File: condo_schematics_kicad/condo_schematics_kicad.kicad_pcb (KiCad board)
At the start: 2 copper layers, 40.6 x 30.5 mm, 3 parts, among them J1 Conn_01x02_Male

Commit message: Adding kicad schematics and PCB
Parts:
- added J10: Conn_01x01_Male, Connector_PinHeader_2.54mm:PinHeader_1x01_P2.54mm_Vertical, F.Cu at (132.1, 109.2)
- added J11: Conn_01x01_Male, Connector_PinHeader_2.54mm:PinHeader_1x01_P2.54mm_Vertical, F.Cu at (61.0, 88.9)
- added J2: Screw_Terminal_01x02, TerminalBlock:TerminalBlock_Altech_AK300-2_P5.00mm, F.Cu at (71.1, 114.3)
- added J3: Conn_01x01_Male, Connector_PinHeader_2.54mm:PinHeader_1x01_P2.54mm_Vertical, F.Cu at (76.2, 88.9)
- added J4: Screw_Terminal_01x02, TerminalBlock:TerminalBlock_Altech_AK300-2_P5.00mm, F.Cu at (88.9, 114.3)
- added J5: Conn_01x01_Male, Connector_PinHeader_2.54mm:PinHeader_1x01_P2.54mm_Vertical, F.Cu at (94.0, 88.9)
- added J6: Screw_Terminal_01x02, TerminalBlock:TerminalBlock_Altech_AK300-2_P5.00mm, F.Cu at (106.7, 114.3)
- added J7: Conn_01x01_Male, Connector_PinHeader_2.54mm:PinHeader_1x01_P2.54mm_Vertical, F.Cu at (111.8, 88.9)
- added J8: Screw_Terminal_01x02, TerminalBlock:TerminalBlock_Altech_AK300-2_P5.00mm, F.Cu at (124.5, 114.3)
- added J9: Conn_01x01_Male, Connector_PinHeader_2.54mm:PinHeader_1x01_P2.54mm_Vertical, F.Cu at (129.5, 88.9)
- added R10: R, Resistor_THT:R_Axial_DIN0207_L6.3mm_D2.5mm_P7.62mm_Horizontal, F.Cu at (106.7, 95.2)
- added R11: 110, Resistor_THT:R_Axial_DIN0207_L6.3mm_D2.5mm_P7.62mm_Horizontal, F.Cu at (119.4, 105.4)
- added R12: R, Resistor_THT:R_Axial_DIN0207_L6.3mm_D2.5mm_P7.62mm_Horizontal, F.Cu at (124.5, 97.8)
- added R13: R, Resistor_THT:R_Axial_DIN0207_L6.3mm_D2.5mm_P7.62mm_Horizontal, F.Cu at (124.5, 95.2)
- added R2: 110, Resistor_THT:R_Axial_DIN0207_L6.3mm_D2.5mm_P7.62mm_Horizontal, F.Cu at (66.0, 105.4)
- added R3: R, Resistor_THT:R_Axial_DIN0207_L6.3mm_D2.5mm_P7.62mm_Horizontal, F.Cu at (71.1, 97.8)
- added R4: R, Resistor_THT:R_Axial_DIN0207_L6.3mm_D2.5mm_P7.62mm_Horizontal, F.Cu at (71.1, 95.2)
- added R5: 110, Resistor_THT:R_Axial_DIN0207_L6.3mm_D2.5mm_P7.62mm_Horizontal, F.Cu at (83.8, 105.4)
- added R6: R, Resistor_THT:R_Axial_DIN0207_L6.3mm_D2.5mm_P7.62mm_Horizontal, F.Cu at (88.9, 97.8)
- added R7: R, Resistor_THT:R_Axial_DIN0207_L6.3mm_D2.5mm_P7.62mm_Horizontal, F.Cu at (88.9, 95.2)
- added R8: 110, Resistor_THT:R_Axial_DIN0207_L6.3mm_D2.5mm_P7.62mm_Horizontal, F.Cu at (101.6, 105.4)
- added R9: R, Resistor_THT:R_Axial_DIN0207_L6.3mm_D2.5mm_P7.62mm_Horizontal, F.Cu at (106.7, 97.8)
- added U1: EL817, Package_DIP:DIP-4_W7.62mm, F.Cu at (64.8, 95.2)
- added U2: EL817, Package_DIP:DIP-4_W7.62mm, F.Cu at (82.5, 95.2)
- added U3: EL817, Package_DIP:DIP-4_W7.62mm, F.Cu at (100.3, 95.2)
- added U4: EL817, Package_DIP:DIP-4_W7.62mm, F.Cu at (118.1, 95.2)
- moved J1 111.8 mm to (268.0, 106.7)
- moved R1 111.8 mm to (237.5, 116.8)
- moved D1 111.8 mm to (243.8, 96.5)
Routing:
- net +3V3: track 0.00 -> 78.3 mm
- net GND: track 0.00 -> 76.2 mm
- net Net-(J6-Pad1): track 0.00 -> 20.6 mm
- net Net-(J8-Pad1): track 0.00 -> 20.6 mm
- net Net-(J2-Pad1): track 0.00 -> 20.6 mm
- net Net-(J4-Pad1): track 0.00 -> 20.6 mm
- net Net-(R10-Pad1): track 0.00 -> 11.8 mm
- net Net-(R3-Pad1): track 0.00 -> 11.8 mm
- net Net-(R12-Pad1): track 0.00 -> 11.8 mm
- net Net-(R6-Pad1): track 0.00 -> 11.7 mm
- net Net-(J6-Pad2): track 0.00 -> 8.92 mm
- net Net-(J4-Pad2): track 0.00 -> 8.92 mm
- net Net-(J8-Pad2): track 0.00 -> 8.92 mm
- net Net-(J2-Pad2): track 0.00 -> 8.92 mm
- net Net-(J9-Pad1): track 0.00 -> 5.61 mm
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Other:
- board size 40.6 x 30.5 mm -> 213.4 x 43.2 mm

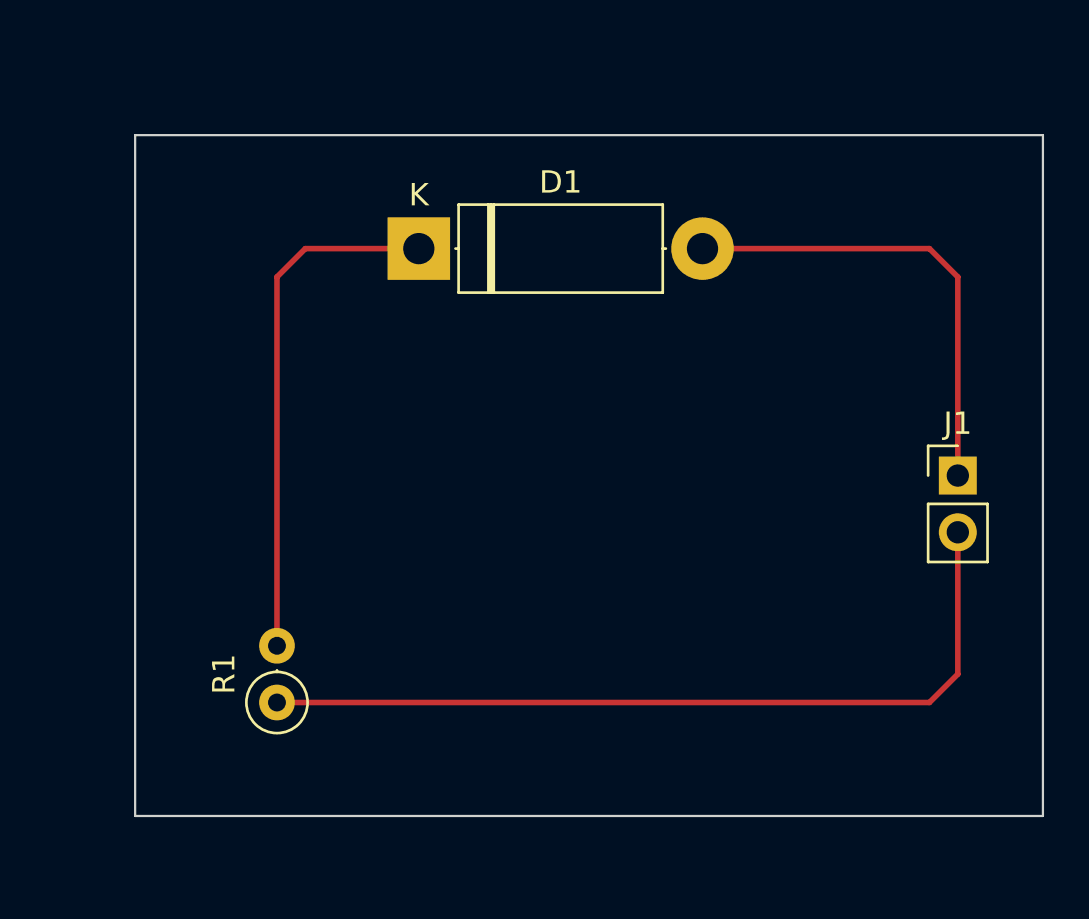
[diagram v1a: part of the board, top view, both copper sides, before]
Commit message: Cleaning test schematics and PCBs
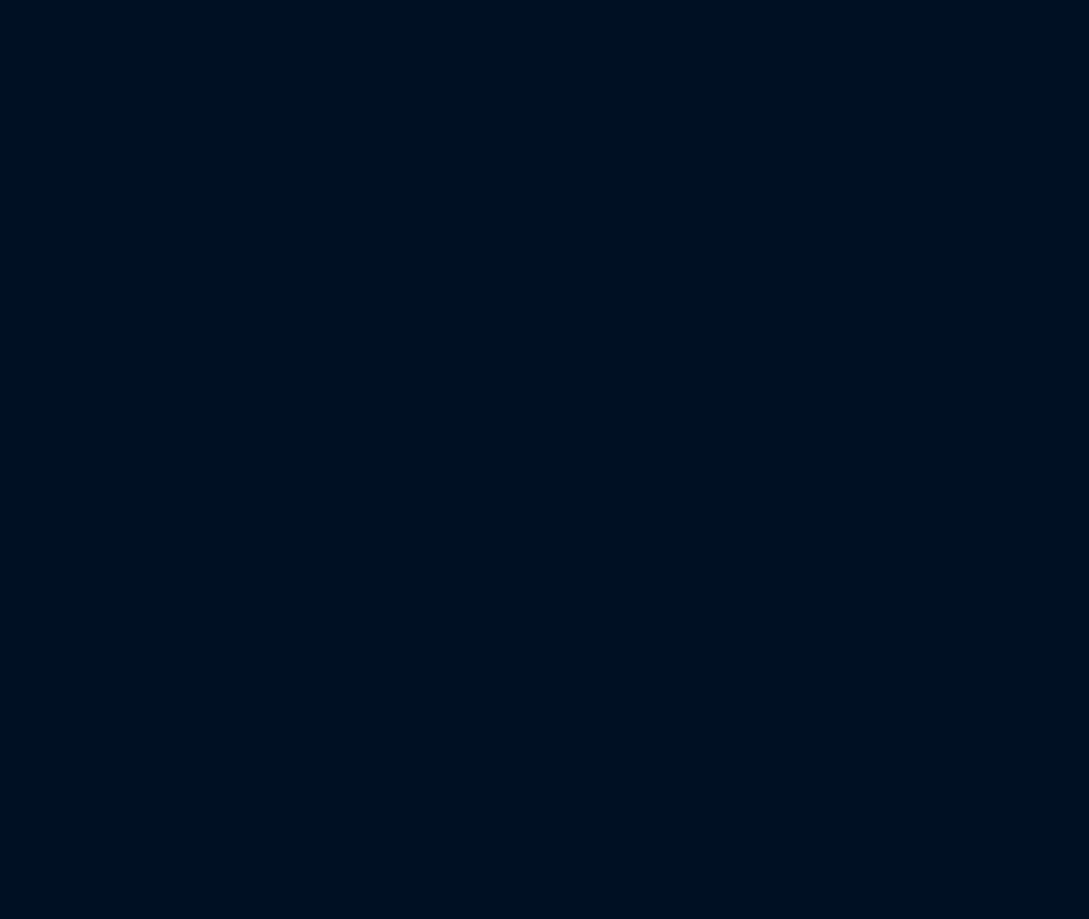
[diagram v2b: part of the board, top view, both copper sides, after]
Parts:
- removed D1: DIODE, Diode_THT:D_5W_P12.70mm_Horizontal
- removed J1: Conn_01x02_Male, Connector_PinHeader_2.54mm:PinHeader_1x02_P2.54mm_Vertical
- removed R1: 570, Resistor_THT:R_Axial_DIN0207_L6.3mm_D2.5mm_P2.54mm_Vertical
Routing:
- net +5V: track 37.4 -> 0.00 mm
- net Net-(D1-Pad1): track 23.4 -> 0.00 mm
- net Earth: track 20.8 -> 0.00 mm
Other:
- board size 213.4 x 43.2 mm -> 76.2 x 43.2 mm
